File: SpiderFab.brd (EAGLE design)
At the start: 69.8 x 50.8 mm, 47 parts, among them IC1 SN754410, J14 5.5x2.1mm Barrel, U1 ATMEGA328, U3 MCP73831, X1 USBSMD, Y1 16MHz

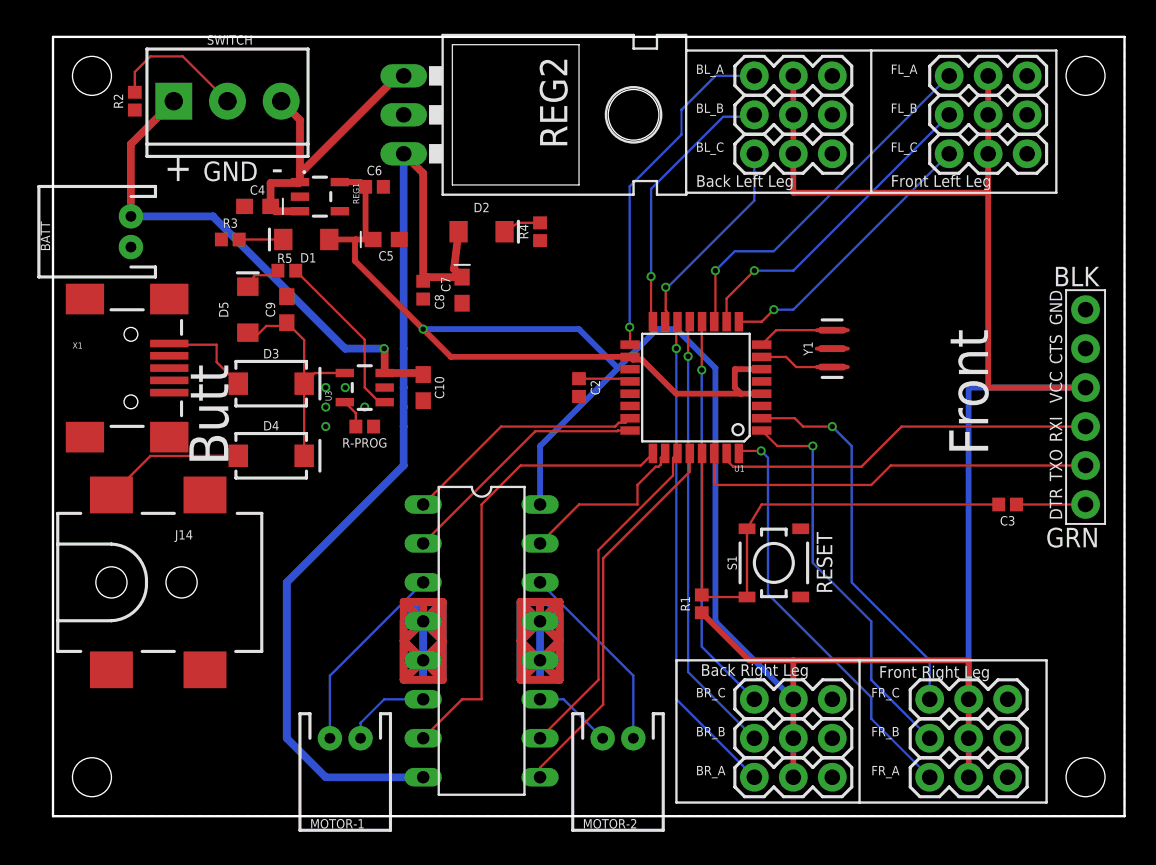
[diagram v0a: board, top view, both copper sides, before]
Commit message: Swap 0402 caps for 0603 package.
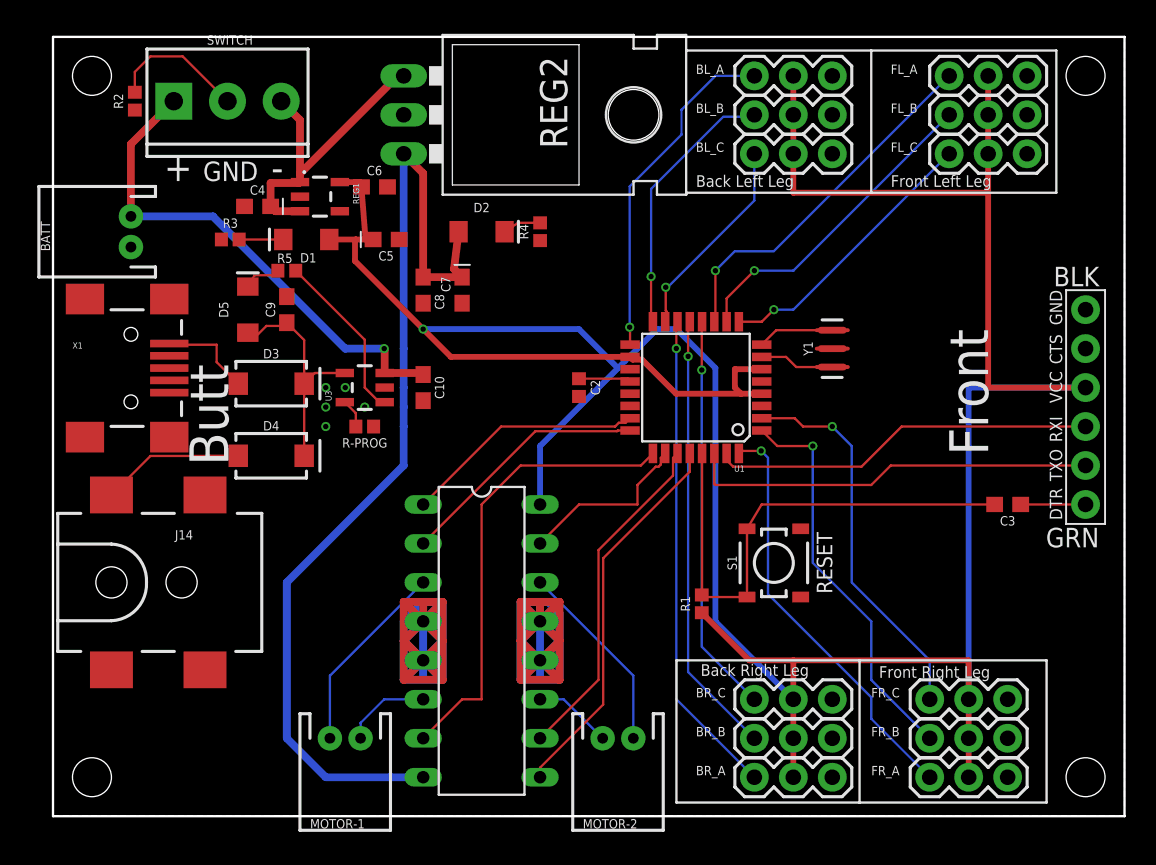
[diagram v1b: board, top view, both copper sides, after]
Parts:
- C3, C6, C8: device SparkFun-Capacitors:0402 -> SparkFun-Capacitors:0603
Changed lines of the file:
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@@
 <attribute name="VALUE" x="33.528" y="27.94" size="0.6096" layer="27" font="vector" ratio="20" rot="R270" align="top-center"/>
 </element>
-<element name="C3" library="SparkFun-Capacitors" library_urn="urn:adsk.eagle:library:510" package="0402" package3d_urn="urn:adsk.eagle:package:37413/1" value="0.1uF" x="62.23" y="20.32" smashed="yes" rot="R180">
+<element name="C3" library="SparkFun-Capacitors" library_urn="urn:adsk.eagle:library:510" package="0603" package3d_urn="urn:adsk.eagle:package:37414/1" value="0.1uF" x="62.23" y="20.32" smashed="yes" rot="R180">
 <attribute name="NAME" x="62.23" y="19.558" size="0.6096" layer="25" font="vector" ratio="20" rot="R180" align="bottom-center"/>
-<attribute name="PROD_ID" value="CAP-12416" x="31.75" y="81.28" size="1.778" layer="27" rot="R180" display="off"/>
+<attribute name="PROD_ID" value="CAP-00810" x="31.75" y="81.28" size="1.778" layer="27" rot="R180" display="off"/>
 <attribute name="VALUE" x="62.23" y="21.082" size="0.6096" layer="27" font="vector" ratio="20" rot="R180" align="top-center"/>
 </element>
@@
 <attribute name="VALUE" x="21.717" y="38.354" size="0.6096" layer="27" font="vector" ratio="20" rot="R180" align="top-center"/>
 </element>
-<element name="C6" library="SparkFun-Capacitors" library_urn="urn:adsk.eagle:library:510" package="0402" package3d_urn="urn:adsk.eagle:package:37413/1" value="0.1uF" x="20.955" y="41.021" smashed="yes">
+<element name="C6" library="SparkFun-Capacitors" library_urn="urn:adsk.eagle:library:510" package="0603" package3d_urn="urn:adsk.eagle:package:37414/1" value="0.1uF" x="20.955" y="41.021" smashed="yes">
 <attribute name="NAME" x="20.955" y="41.783" size="0.6096" layer="25" font="vector" ratio="20" align="bottom-center"/>
-<attribute name="PROD_ID" value="CAP-12416" x="55.245" y="-19.939" size="1.778" layer="27" display="off"/>
+<attribute name="PROD_ID" value="CAP-00810" x="55.245" y="-19.939" size="1.778" layer="27" display="off"/>
 <attribute name="VALUE" x="20.955" y="40.259" size="0.6096" layer="27" font="vector" ratio="20" align="top-center"/>
 </element>
@@
 <attribute name="VALUE" x="27.432" y="34.29" size="0.6096" layer="27" font="vector" ratio="20" rot="R90" align="top-center"/>
 </element>
-<element name="C8" library="SparkFun-Capacitors" library_urn="urn:adsk.eagle:library:510" package="0402" package3d_urn="urn:adsk.eagle:package:37413/1" value="0.1uF" x="24.13" y="34.29" smashed="yes" rot="R270">
+<element name="C8" library="SparkFun-Capacitors" library_urn="urn:adsk.eagle:library:510" package="0603" package3d_urn="urn:adsk.eagle:package:37414/1" value="0.1uF" x="24.13" y="34.29" smashed="yes" rot="R270">
 <attribute name="NAME" x="24.892" y="33.528" size="0.6096" layer="25" font="vector" ratio="20" rot="R270" align="bottom-center"/>
-<attribute name="PROD_ID" value="CAP-12416" x="-36.83" y="-3.81" size="1.778" layer="27" rot="R270" display="off"/>
+<attribute name="PROD_ID" value="CAP-00810" x="-36.83" y="-3.81" size="1.778" layer="27" rot="R270" display="off"/>
 <attribute name="VALUE" x="23.368" y="34.29" size="0.6096" layer="27" font="vector" ratio="20" rot="R270" align="top-center"/>
 </element>
@@
 <wire x1="42.291" y1="13.263" x2="45.394" y2="10.16" width="0.381" layer="1"/>
 <wire x1="45.394" y1="10.16" x2="48.26" y2="10.16" width="0.381" layer="1"/>
-<wire x1="20.375" y1="37.592" x2="20.375" y2="41.021" width="0.381" layer="1"/>
-<wire x1="20.375" y1="41.021" x2="20.06" y2="41.336" width="0.381" layer="1"/>
+<wire x1="20.375" y1="37.592" x2="20.105" y2="41.021" width="0.381" layer="1"/>
+<wire x1="20.105" y1="41.021" x2="20.06" y2="41.336" width="0.381" layer="1"/>
 <wire x1="20.06" y1="41.336" x2="18.6991" y2="41.336" width="0.381" layer="1"/>
 <wire x1="20.375" y1="37.592" x2="19.74" y2="37.592" width="0.381" layer="1"/>
@@
 <contactref element="J1" pad="P$1"/>
 <contactref element="C3" pad="1"/>
-<wire x1="62.81" y1="20.32" x2="67.31" y2="20.32" width="0.1524" layer="1"/>
+<wire x1="63.08" y1="20.32" x2="67.31" y2="20.32" width="0.1524" layer="1"/>
 </signal>
 <signal name="RESET">
@@
 <wire x1="42.31" y1="14.809175" x2="42.31" y2="23.6474" width="0.1524" layer="1"/>
 <wire x1="45.24" y1="18.735" x2="46.195" y2="20.32" width="0.1524" layer="1"/>
-<wire x1="46.195" y1="20.32" x2="61.65" y2="20.32" width="0.1524" layer="1"/>
+<wire x1="46.195" y1="20.32" x2="61.38" y2="20.32" width="0.1524" layer="1"/>
 <wire x1="42.291" y1="14.423" x2="42.429" y2="14.285" width="0.1524" layer="1"/>
 <wire x1="42.429" y1="14.285" x2="45.24" y2="14.285" width="0.1524" layer="1"/>
@@
 <wire x1="22.86" y1="25.4" x2="22.86" y2="22.86" width="0.508" layer="16"/>
 <wire x1="26.67" y1="35.14" x2="24.4" y2="35.14" width="0.508" layer="1"/>
-<wire x1="24.4" y1="35.14" x2="24.13" y2="34.87" width="0.508" layer="1"/>
-<wire x1="24.13" y1="34.87" x2="24.13" y2="41.91" width="0.508" layer="1"/>
+<wire x1="24.4" y1="35.14" x2="24.13" y2="35.14" width="0.508" layer="1"/>
+<wire x1="24.13" y1="35.14" x2="24.13" y2="41.91" width="0.508" layer="1"/>
 <wire x1="24.13" y1="41.91" x2="22.86" y2="43.18" width="0.508" layer="1"/>
 <wire x1="26.67" y1="35.14" x2="26.14" y2="35.67" width="0.508" layer="1"/>

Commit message: Change footprint for diodes and resistors.
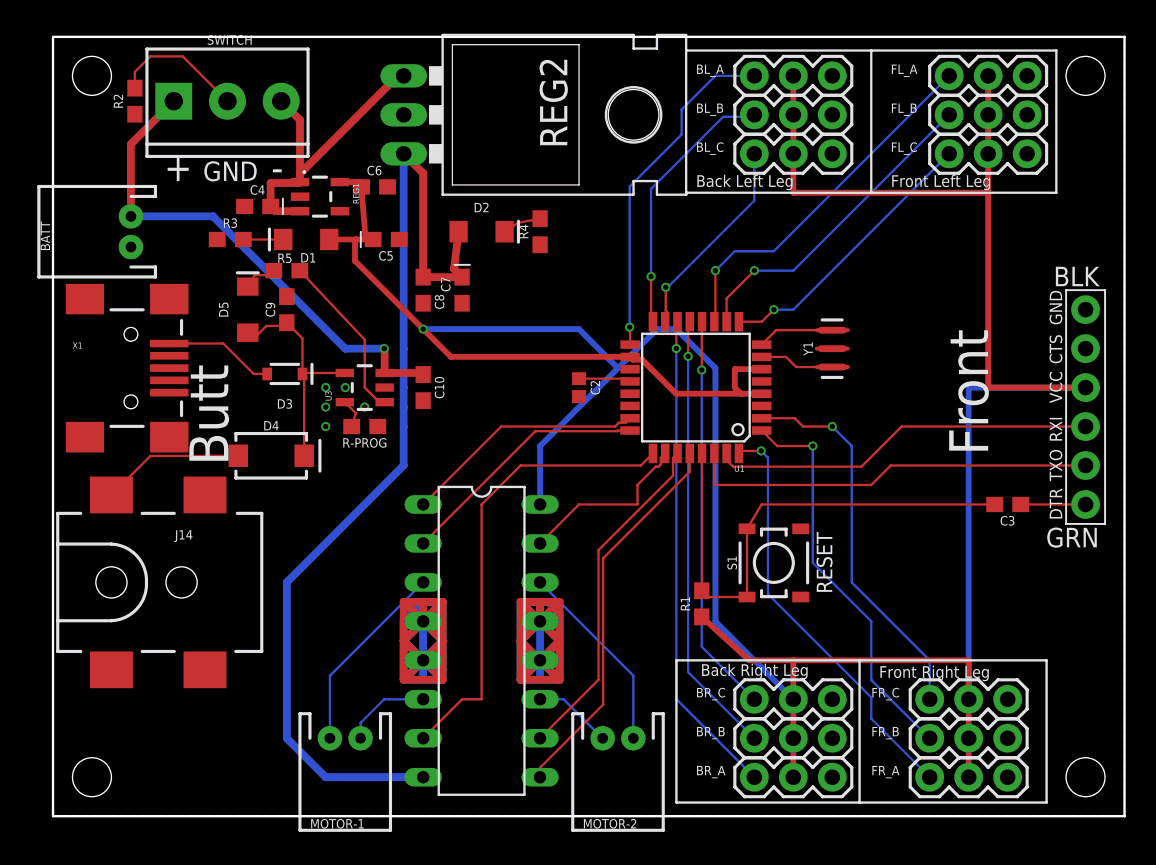
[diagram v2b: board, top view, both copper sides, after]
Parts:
- D3: device SparkFun-DiscreteSemi:SMA-DIODE -> SparkFun-DiscreteSemi:SOD-323
- R-PROG: value 1K -> 1k; device SparkFun-Resistors:0402 -> SparkFun-Resistors:0603
- R1, R3: value 10K -> 10k; device SparkFun-Resistors:0402 -> SparkFun-Resistors:0603
- R2, R4: value (none) -> 10k; device SparkFun-Resistors:0402 -> SparkFun-Resistors:0603
- R5: device SparkFun-Resistors:0402 -> SparkFun-Resistors:0603
- moved D3 1.09 mm to (15.1, 28.8), turned to 180 degrees
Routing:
- net N$8: track 6.24 -> 7.20 mm

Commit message: Replace internal connectors with vertical JST.
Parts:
- MOTOR-1, MOTOR-2: device SparkFun-Connectors:JST-2-PTH -> adafruit:JST-PH-2-THM
- SWITCH: device SparkFun-Connectors:SCREWTERMINAL-3.5MM-3 -> SparkFun-Connectors:JST-3-PTH-VERT
- moved SWITCH 2.54 mm to (10.4, 46.6)
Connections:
- net N$3: now also MOTOR-1.1; no longer MOTOR-1.2
- net N$5: now also MOTOR-1.2; no longer MOTOR-1.1
- net N$6: now also MOTOR-2.2; no longer MOTOR-2.1
- net N$7: now also MOTOR-2.1; no longer MOTOR-2.2
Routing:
- net N$11: track 8.73 -> 5.66 mm
- net RAW: track 21.2 -> 23.5 mm
- net BATT+: track 32.9 -> 32.1 mm
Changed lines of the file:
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@@
 <attribute name="VALUE" x="55.88" y="3.048" size="0.6096" layer="27" font="vector" ratio="20"/>
 </element>
-<element name="MOTOR-1" library="SparkFun-Connectors" library_urn="urn:adsk.eagle:library:513" package="JST-2-PTH" package3d_urn="urn:adsk.eagle:package:38053/1" value="" x="19.05" y="5.08" smashed="yes" rot="R180">
-<attribute name="NAME" x="20.32" y="-0.19" size="0.6096" layer="25" font="vector" ratio="20" rot="R180"/>
-<attribute name="PROD_ID" value="CONN-09863" x="-40.64" y="27.94" size="1.778" layer="27" rot="R180" display="off"/>
-<attribute name="SKU" value="PRT-09914" x="-40.64" y="27.94" size="1.778" layer="27" rot="R180" display="off"/>
+<element name="MOTOR-1" library="adafruit" library_urn="urn:adsk.eagle:library:420" package="JST-PH-2-THM" package3d_urn="urn:adsk.eagle:package:6240693/1" value="" x="19.05" y="5.08" smashed="yes" rot="R180">
+<attribute name="NAME" x="20.574" y="1.969" size="0.6096" layer="25" font="vector" ratio="20" rot="R180"/>
 <attribute name="VALUE" x="20.32" y="2.35" size="0.6096" layer="27" font="vector" ratio="20" rot="R180"/>
 </element>
-<element name="MOTOR-2" library="SparkFun-Connectors" library_urn="urn:adsk.eagle:library:513" package="JST-2-PTH" package3d_urn="urn:adsk.eagle:package:38053/1" value="" x="36.83" y="5.08" smashed="yes" rot="R180">
-<attribute name="NAME" x="38.1" y="-0.19" size="0.6096" layer="25" font="vector" ratio="20" rot="R180"/>
-<attribute name="PROD_ID" value="CONN-09863" x="20.32" y="39.37" size="1.778" layer="27" rot="R180" display="off"/>
-<attribute name="SKU" value="PRT-09914" x="20.32" y="39.37" size="1.778" layer="27" rot="R180" display="off"/>
+<element name="MOTOR-2" library="adafruit" library_urn="urn:adsk.eagle:library:420" package="JST-PH-2-THM" package3d_urn="urn:adsk.eagle:package:6240693/1" value="" x="36.83" y="5.08" smashed="yes" rot="R180">
+<attribute name="NAME" x="38.481" y="1.969" size="0.6096" layer="25" font="vector" ratio="20" rot="R180"/>
 <attribute name="VALUE" x="38.1" y="2.35" size="0.6096" layer="27" font="vector" ratio="20" rot="R180"/>
 </element>
@@
 <attribute name="PROD_ID" value="SWCH-09213" x="82.55" y="45.72" size="1.778" layer="27" rot="R90" display="off"/>
 </element>
-<element name="SWITCH" library="SparkFun-Connectors" library_urn="urn:adsk.eagle:library:513" package="SCREWTERMINAL-3.5MM-3" package3d_urn="urn:adsk.eagle:package:38072/1" value="" x="7.874" y="46.609" smashed="yes">
-<attribute name="NAME" x="10.033" y="50.292" size="0.6096" layer="25" font="vector" ratio="20"/>
-<attribute name="PROD_ID" value="CONN-08288" x="53.594" y="21.209" size="1.778" layer="27" display="off"/>
-<attribute name="SF_ID" value="PRT-08235" x="53.594" y="21.209" size="1.778" layer="27" display="off"/>
-<attribute name="VALUE" x="9.906" y="42.037" size="0.6096" layer="27" font="vector" ratio="20"/>
+<element name="SWITCH" library="SparkFun-Connectors" library_urn="urn:adsk.eagle:library:513" package="JST-3-PTH-VERT" package3d_urn="urn:adsk.eagle:package:38080/1" value="" x="10.414" y="46.609" smashed="yes">
+<attribute name="NAME" x="8.763" y="49.022" size="0.6096" layer="25" font="vector" ratio="20"/>
+<attribute name="PROD_ID" value="CONN-13230" x="56.134" y="21.209" size="1.778" layer="27" display="off"/>
+<attribute name="VALUE" x="12.446" y="42.037" size="0.6096" layer="27" font="vector" ratio="20"/>
 </element>
 <element name="U1" library="SparkFun" package="TQFP32-08" value="ATMEGA328" x="41.91" y="27.94" smashed="yes" rot="R180">
@@
 <signal name="N$3">
 <contactref element="IC1" pad="3"/>
-<contactref element="MOTOR-1" pad="2"/>
+<contactref element="MOTOR-1" pad="1"/>
 <wire x1="24.13" y1="15.24" x2="18.05" y2="9.16" width="0.1524" layer="16"/>
 <wire x1="18.05" y1="9.16" x2="18.05" y2="5.08" width="0.1524" layer="16"/>
@@
 <signal name="N$5">
 <contactref element="IC1" pad="6"/>
-<contactref element="MOTOR-1" pad="1"/>
+<contactref element="MOTOR-1" pad="2"/>
 <wire x1="24.13" y1="7.62" x2="21.59" y2="7.62" width="0.1524" layer="16"/>
 <wire x1="21.59" y1="7.62" x2="20.05" y2="6.08" width="0.1524" layer="16"/>
@@
 <signal name="N$6">
 <contactref element="IC1" pad="14"/>
-<contactref element="MOTOR-2" pad="1"/>
+<contactref element="MOTOR-2" pad="2"/>
 <wire x1="31.75" y1="15.24" x2="37.83" y2="9.16" width="0.1524" layer="16"/>
 <wire x1="37.83" y1="9.16" x2="37.83" y2="5.08" width="0.1524" layer="16"/>
@@
 <signal name="N$7">
 <contactref element="IC1" pad="11"/>
-<contactref element="MOTOR-2" pad="2"/>
+<contactref element="MOTOR-2" pad="1"/>
 <wire x1="31.75" y1="7.62" x2="33.29" y2="7.62" width="0.1524" layer="16"/>
 <wire x1="33.29" y1="7.62" x2="35.83" y2="5.08" width="0.1524" layer="16"/>
@@
 <wire x1="14.185" y1="41.275" x2="16.0379" y2="41.275" width="0.508" layer="1"/>
 <wire x1="16.0379" y1="41.275" x2="16.0989" y2="41.336" width="0.508" layer="1"/>
-<wire x1="16.0989" y1="41.336" x2="16.0989" y2="45.3841" width="0.508" layer="1"/>
-<wire x1="16.0989" y1="45.3841" x2="14.874" y2="46.609" width="0.508" layer="1"/>
+<wire x1="16.0989" y1="41.336" x2="16.0989" y2="45.659484375" width="0.508" layer="1"/>
+<wire x1="16.0989" y1="45.659484375" x2="15.24349375" y2="45.752228125" width="0.508" layer="1"/>
+<wire x1="15.24349375" y1="45.752228125" x2="12.414" y2="46.059" width="0.508" layer="1"/>
 <wire x1="16.0989" y1="39.436" x2="14.5" y2="39.436" width="0.508" layer="1"/>
 <wire x1="14.5" y1="39.436" x2="14.185" y2="39.751" width="0.508" layer="1"/>
@@
 <wire x1="21.59" y1="30.48" x2="21.6201" y2="30.4499" width="0.508" layer="1"/>
 <wire x1="21.6201" y1="30.4499" x2="21.6201" y2="28.89" width="0.508" layer="1"/>
-<wire x1="5.08" y1="39.1" x2="5.08" y2="43.815" width="0.508" layer="1"/>
-<wire x1="5.08" y1="43.815" x2="7.874" y2="46.609" width="0.508" layer="1"/>
+<wire x1="5.08" y1="39.1" x2="6.429" y2="40.449" width="0.508" layer="1"/>
+<wire x1="8.414" y1="46.059" x2="6.429" y2="40.449" width="0.508" layer="1"/>
 </signal>
 <signal name="N$11">
 <contactref element="SWITCH" pad="2"/>
 <contactref element="R2" pad="2"/>
-<wire x1="5.334" y1="47.459" x2="5.334" y2="48.514" width="0.1524" layer="1"/>
-<wire x1="5.334" y1="48.514" x2="6.35" y2="49.53" width="0.1524" layer="1"/>
-<wire x1="6.35" y1="49.53" x2="8.453" y2="49.53" width="0.1524" layer="1"/>
-<wire x1="8.453" y1="49.53" x2="11.374" y2="46.609" width="0.1524" layer="1"/>
+<wire x1="5.334" y1="47.459" x2="9.014" y2="47.459" width="0.1524" layer="1"/>
+<wire x1="9.014" y1="47.459" x2="10.414" y2="46.059" width="0.1524" layer="1"/>
 </signal>
 <signal name="N$9">
